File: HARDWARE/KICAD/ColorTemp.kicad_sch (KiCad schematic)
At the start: 27 parts, among them J1 POWER, J2 Conn_02x05_Odd_Even, SW1 USER, SW2 ~{RESET}, U1 CH32V003F4U6, U2 MCP9700A

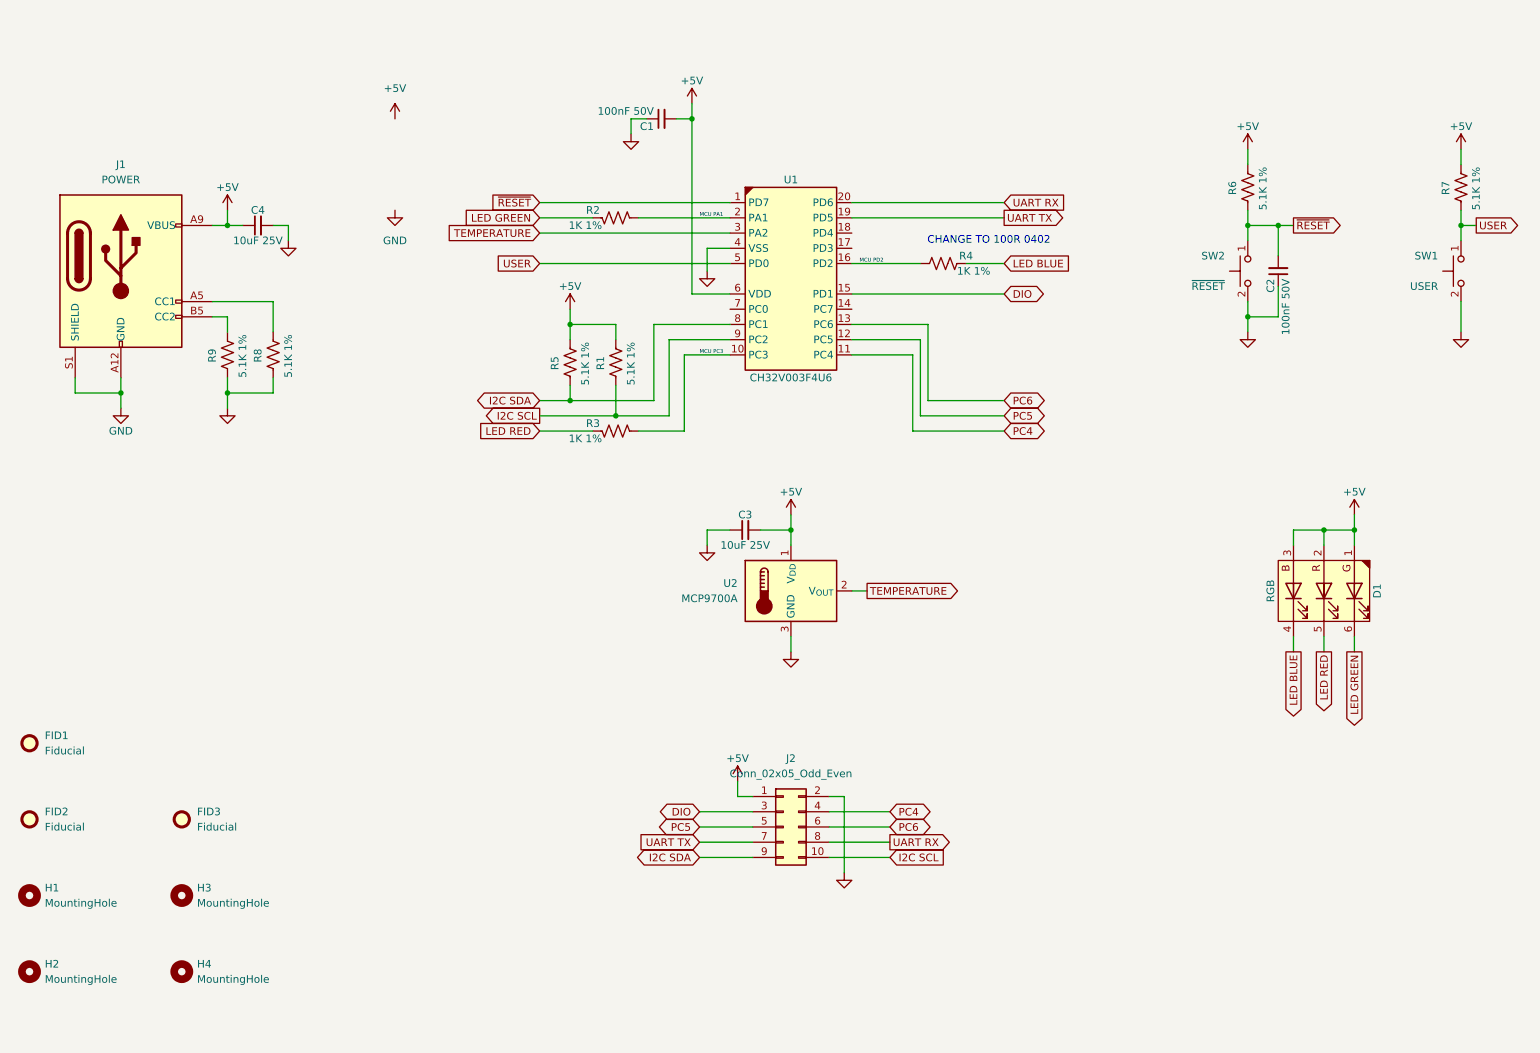
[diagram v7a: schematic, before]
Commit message: Renumbering, PWR_FLAG, schematic detailing.
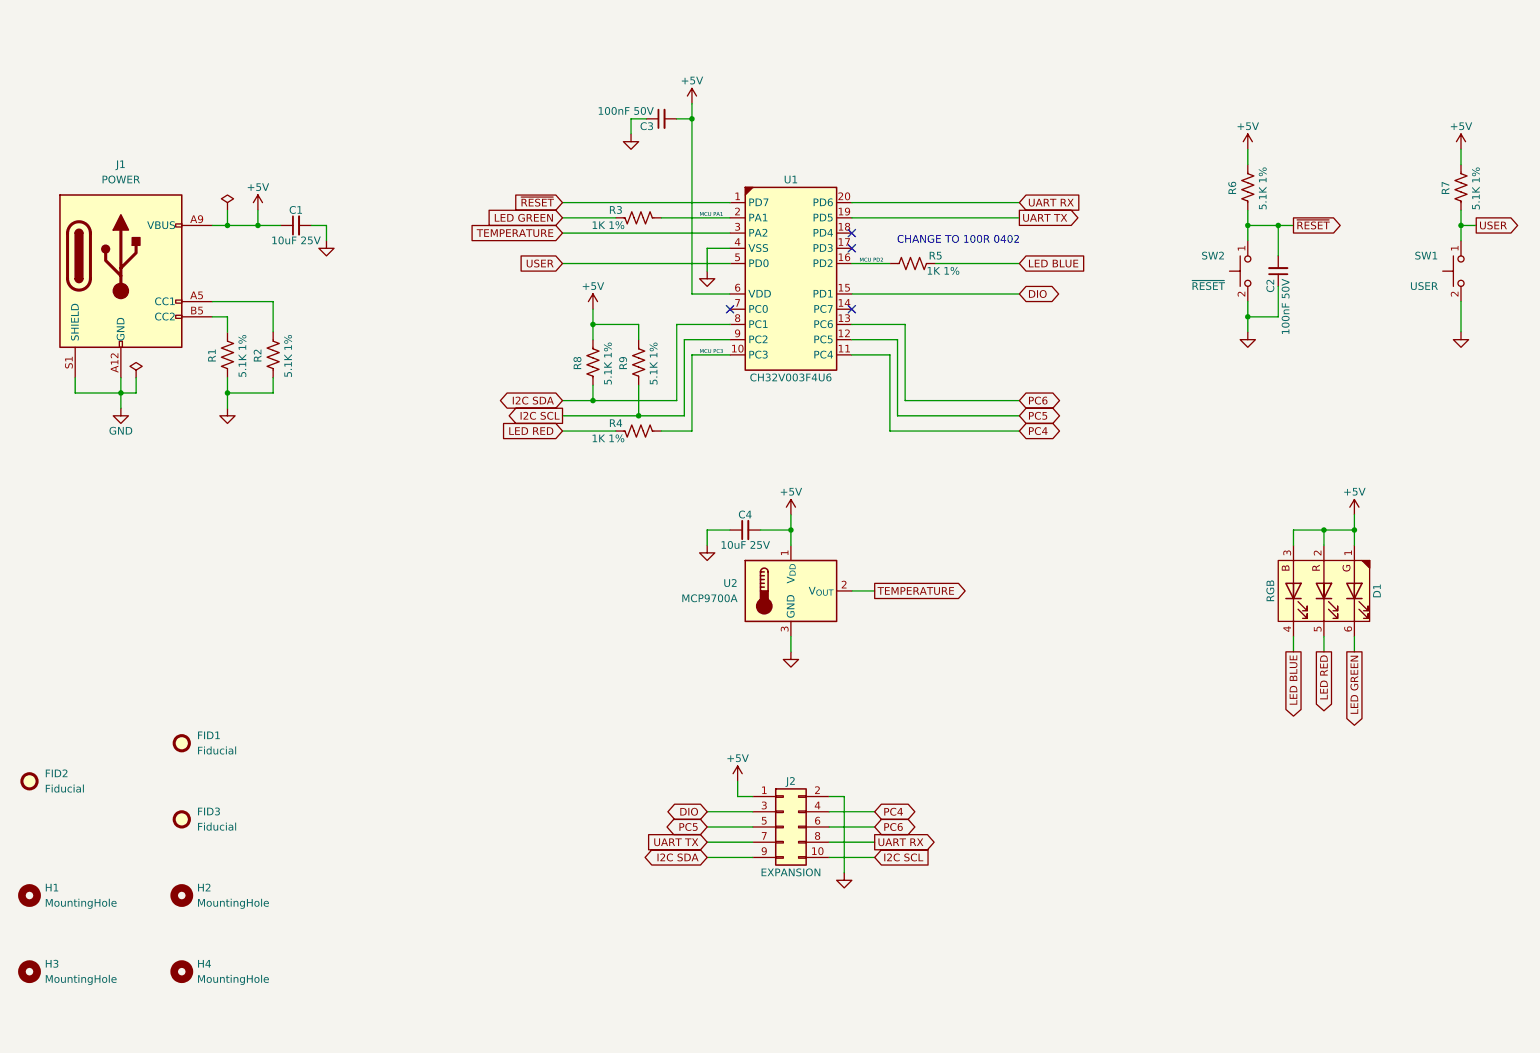
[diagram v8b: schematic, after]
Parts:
- J2: value Conn_02x05_Odd_Even -> EXPANSION
- renumbered C4 to C1, C1 to C3, C3 to C4, FID2 to FID1, FID1 to FID2, H3 to H1, H1 to H2, H4 to H3, H2 to H4, R9 to R1, R8 to R2, R2 to R3, R3 to R4, R4 to R5, R5 to R8, R1 to R9
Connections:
- no-connect marks 0 -> 4
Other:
- moved on the sheet: C1, FID1, FID2, H1, H2, H3, H4, R3, R4, R5, R8, R9
